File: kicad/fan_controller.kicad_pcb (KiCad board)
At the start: 2 copper layers, 98.8 x 17.8 mm, 50 parts, among them P1 CONN_01X04, P2 CONN_01X05, P3 CONN_01X04, P4 CONN_01X04, P5 CONN_01X04, P6 CONN_01X04, Q1 Q_NPN_BEC, Q2 Q_NPN_BEC, Q3 Q_NPN_BEC, Q4 Q_NPN_BEC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

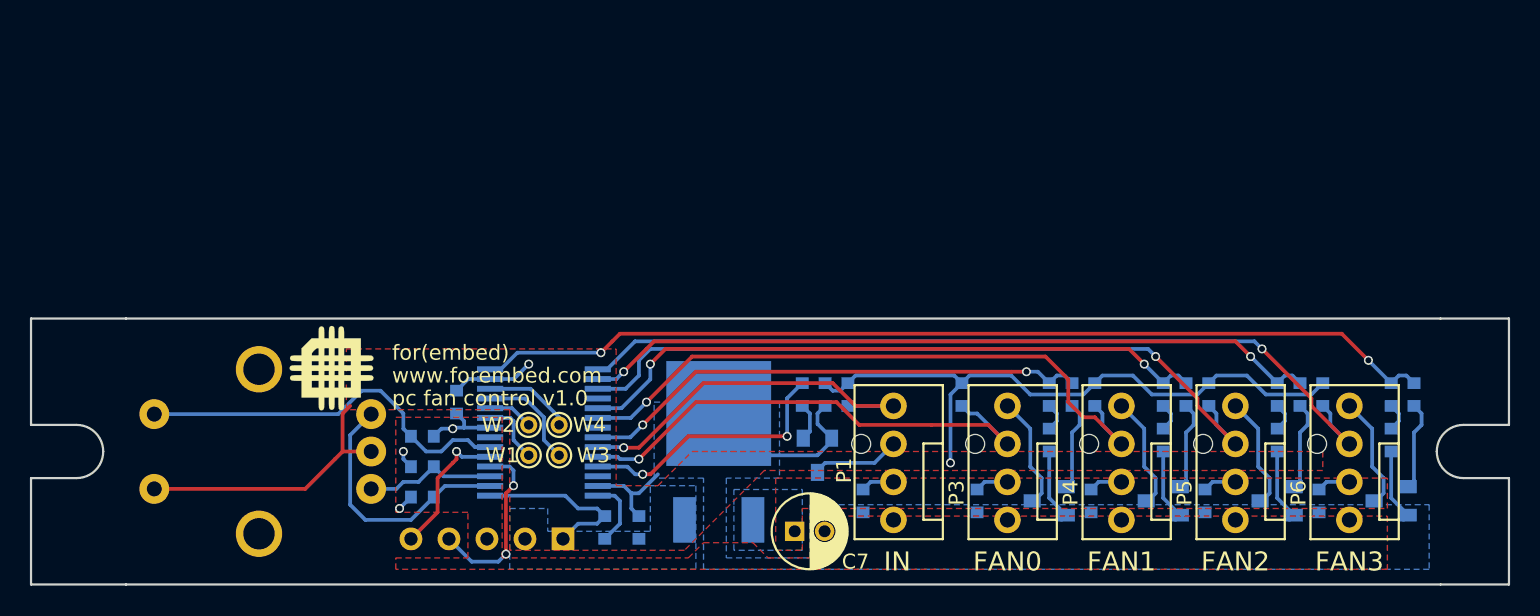
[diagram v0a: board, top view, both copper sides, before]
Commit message: Added hardware files for v1.1 schematic and board
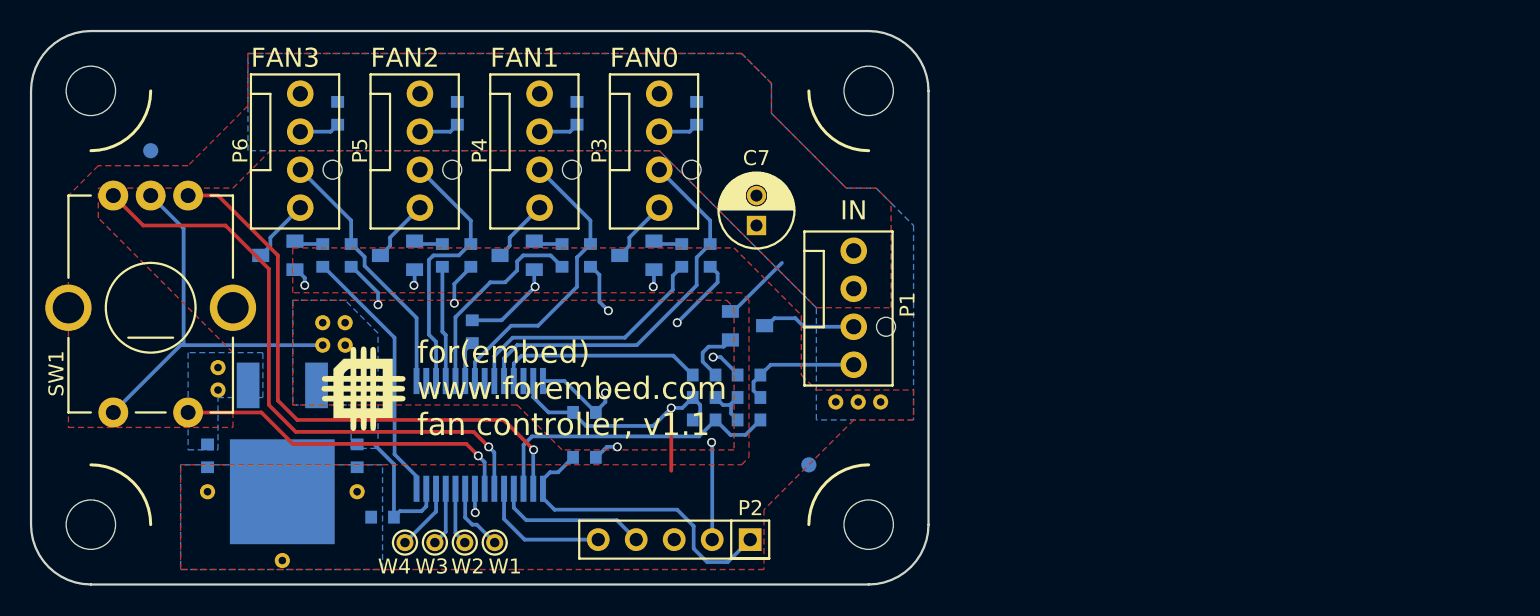
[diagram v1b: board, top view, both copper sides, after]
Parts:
- removed D1, D2, D3, D4: LED, lib_pcb:led_0603
- removed R5: 10k, kicad_pcb:SM_0603
- removed R6, R7, R8, R9: 1k, kicad_pcb:SM_0603
- added C10: 100nF, lib_pcb:SM_0603, B.Cu at (154.0, 78.4)
- added C11: 100nF, lib_pcb:SM_0603, B.Cu at (154.0, 79.9)
- added C12: 1uF, lib_pcb:SM_0603, B.Cu at (138.5, 74.0)
- added REF**: VIA, lib_pcb:VIA, F.Cu at (121.5, 77.9)
- added REF**: VIA, lib_pcb:VIA, F.Cu at (128.5, 74.9)
- added REF**: VIA, lib_pcb:VIA, F.Cu at (130.0, 73.4)
- added REF**: VIA, lib_pcb:VIA, F.Cu at (128.5, 73.4)
- added REF**: MountingHole_0.13in, lib_pcb:MountingHole_0.13in, F.Cu at (165.0, 57.9)
- added REF**: MountingHole_0.13in, lib_pcb:MountingHole_0.13in, F.Cu at (165.0, 86.9)
- added REF**: MountingHole_0.13in, lib_pcb:MountingHole_0.13in, F.Cu at (113.0, 86.9)
- added REF**: MountingHole_0.13in, lib_pcb:MountingHole_0.13in, F.Cu at (113.0, 57.9)
- added REF**: fiducial, lib_pcb:fiducial, B.Cu at (161.0, 82.9)
- added REF**: fiducial, lib_pcb:fiducial, B.Cu at (117.0, 61.9)
- added REF**: VIA, lib_pcb:VIA, F.Cu at (121.5, 76.4)
- added REF**: VIA, lib_pcb:VIA, F.Cu at (165.8, 78.7)
- added REF**: VIA, lib_pcb:VIA, F.Cu at (164.3, 78.7)
- added REF**: VIA, lib_pcb:VIA, F.Cu at (162.8, 78.7)
- added REF**: VIA, lib_pcb:VIA, F.Cu at (130.8, 84.7)
- added REF**: VIA, lib_pcb:VIA, F.Cu at (125.8, 89.3)
- added REF**: VIA, lib_pcb:VIA, F.Cu at (120.8, 84.7)
- added REF**: VIA, lib_pcb:VIA, F.Cu at (130.0, 74.9)
- P2, SW1: moved to F.Cu
- R2: value 10k -> 1k
- U1: value pic24f08km202 -> pic24fv08km202
- moved Q5 76.2 mm to (125.5, 68.9)
- moved R18 73.5 mm to (128.5, 68.9), turned to 270 degrees
- moved P6 73.2 mm to (127.0, 61.9), turned to 90 degrees
- moved C6 70.5 mm to (129.5, 59.4), turned to 90 degrees
- moved R13 65.6 mm to (130.4, 68.9), turned to 90 degrees
- moved Q4 61.1 mm to (133.5, 68.9)
- moved P5 58.4 mm to (135.0, 61.9), turned to 90 degrees
- moved R17 58.1 mm to (136.5, 68.9), turned to 270 degrees
- moved C5 56.3 mm to (137.5, 59.4), turned to 90 degrees
- moved R12 50.2 mm to (138.4, 68.9), turned to 90 degrees
- moved Q3 46.2 mm to (141.5, 68.9)
- moved P4 44.1 mm to (143.0, 61.9), turned to 90 degrees
- moved C1 43.9 mm to (120.8, 82.3)
- moved C4 43.0 mm to (145.5, 59.4), turned to 90 degrees
- moved R16 42.7 mm to (144.5, 68.9), turned to 270 degrees
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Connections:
- net /pwm1 renamed /pwm1(OC5)
- net /pwm3 renamed /pwm3(OC1E)
- net /sense0 renamed /sense0(CN13)
- net /sense_out renamed Net-(R14-Pad1)
- P1 pad 4: pwm_in -> /pwm_in
- R15 pad 2: /pwm0 -> /pwm0(OC2B)
- R17 pad 2: /pwm2 -> /pwm2(OC4)
- R2 pad 2: pwm_in -> /pwm_in
- R3 pad 1: Net-(R3-Pad1) -> Net-(C10-Pad1)
- R3 pad 2: GND -> /pwm_in
- R4 pad 1: Net-(R4-Pad1) -> analog_cmd
- R4 pad 2: GND -> Net-(C10-Pad1)
- SW1 pad 1: Net-(R3-Pad1) -> /ENC_A(CN2)
- SW1 pad 3: Net-(R4-Pad1) -> /ENC_B(CN6)
- SW1 pad 5: Net-(R5-Pad1) -> /SW(CN7)
- U1 pad 16: /pwm2 -> (no net)
- U1 pad 18: (no net) -> /pwm2(OC4)
- U1 pad 2: Net-(R3-Pad1) -> /ENC_A(CN2)
- U1 pad 20: /sense1 -> Net-(C12-Pad1)
- U1 pad 21: (no net) -> /sense1
- U1 pad 22: /pwm0 -> (no net)
- U1 pad 23: pwm_in -> /pwm0(OC2B)
- U1 pad 3: Net-(R4-Pad1) -> analog_cmd
- U1 pad 6: Net-(R5-Pad1) -> /ENC_B(CN6)
- U1 pad 7: (no net) -> /SW(CN7)
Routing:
- net /pwm2: track 49.6 -> 0.00 mm, vias 2 -> 0
- net /pwm3(OC1E): track 64.5 -> 17.5 mm, vias 2 -> 0
- net /ENC_B(CN6): track 0.00 -> 40.3 mm, vias 0 -> 1
- net /sense3: track 57.4 -> 17.4 mm, vias 1 -> 0
- net /ENC_A(CN2): track 0.00 -> 38.4 mm, vias 0 -> 1
- net /pwm0: track 34.3 -> 0.00 mm, vias 2 -> 0
- net /sense2: track 50.5 -> 17.9 mm, vias 1 -> 0
- net /pwm1(OC5): track 42.9 -> 13.8 mm, vias 2 -> 0
- net pwm_in: track 26.0 -> 0.00 mm, vias 1 -> 0
- net Net-(R5-Pad1): track 25.9 -> 0.00 mm
- net /sense1: track 43.3 -> 19.8 mm, vias 1 -> 0
- net /SW(CN7): track 0.00 -> 23.0 mm, vias 0 -> 1
- net analog_cmd: track 0.00 -> 20.3 mm
- net Net-(R3-Pad1): track 17.4 -> 0.00 mm
- net /pwm0(OC2B): track 0.00 -> 17.2 mm
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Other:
- board size 98.8 x 17.8 mm -> 60 x 37 mm
- rule pad_to_mask_clearance: 0.2 -> 0.07
- board text added: "12V"
- board text added: "GND"
- board text added: "PWM"
- board text added: "TACH"
- board text added: "for(embed) www.forembed.com fan controller, v1.1"
- board text removed: "for(embed)"
- board text removed: "pc fan control v1.0"
- board text removed: "www.forembed.com"
